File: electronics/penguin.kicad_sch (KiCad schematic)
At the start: 137 parts, among them IC1 HY2120-AB, J1 USB_C_CONN, J10 MTR_HEADER_2, J2 CAM_HEADER, J3 BATT_BALANCE_HEADER, J4 TOF_HEADER, J6 IR_HEADER_1, J7 IR_HEADER_2, J8 BATT_CONN, J9 MTR_HEADER_1, Q1 AO3400A, Q2 SI2393DS, Q3 2N7002, Q4 FS8205A, SW1 SW_Boot, SW2 SW_Reset, U1 ESP32-S3-WROOM-1U-N8R8, U2 LP5907MFX-2.8, U3 LP5907MFX-1.2, U4 DRV8833PW, U5 MCP23017_ML, U6 TPS5405DR, U7 AMS1117-3.3, U8 DMP4065S-7

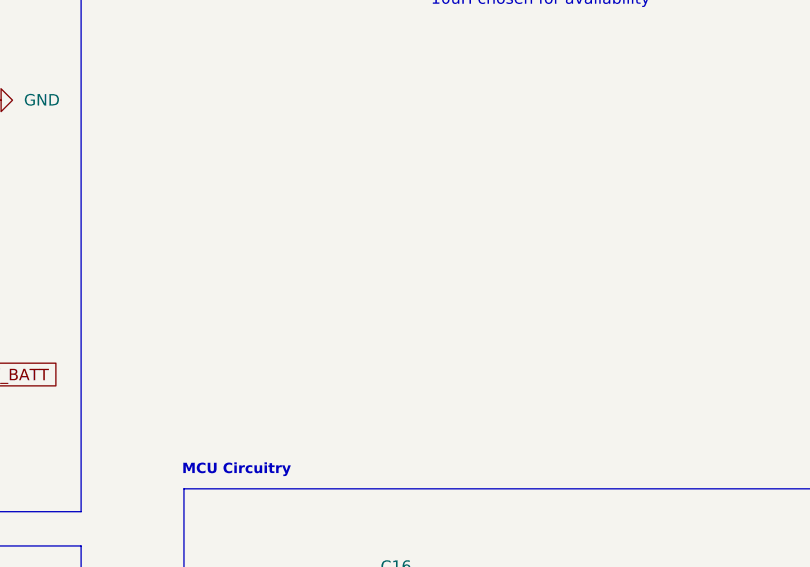
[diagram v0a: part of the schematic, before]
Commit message: finalize board outline
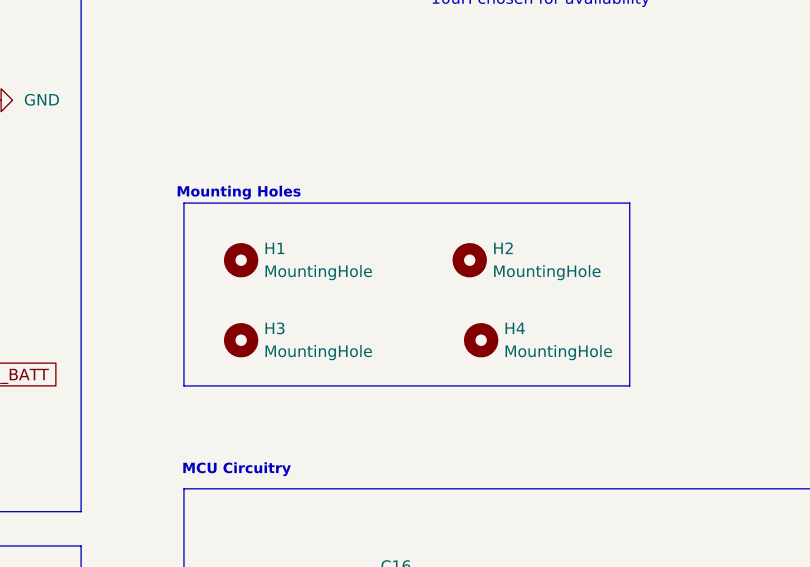
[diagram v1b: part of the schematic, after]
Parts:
- added H1, H2, H3, H4: MountingHole, MountingHole:MountingHole_2.2mm_M2, symbol Mechanical:MountingHole
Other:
- note added: "Mounting Holes"
- company: MREN 178 Course Project Extension -> Jeevan Sanchez
- title: P.A.N. Controller -> Penguin Controller

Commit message: silkscreen
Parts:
- C26: footprint Capacitor_SMD:C_0603_1608Metric -> Capacitor_SMD:C_0805_2012Metric; JLCPCB C14663 -> C49678
- C40: footprint EEH_ZK1V101XP:CAP_EEHZK1V101XP -> EEE_FK1V101P:CAP_EEEFK1V101P
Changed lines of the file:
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@@
 			)
 		)
-		(property "Footprint" "Capacitor_SMD:C_0603_1608Metric"
+		(property "Footprint" "Capacitor_SMD:C_0805_2012Metric"
 			(at 125.4252 86.36 0)
 			(effects
@@
 			)
 		)
-		(property "JLCPCB" "C14663"
+		(property "JLCPCB" "C49678"
 			(at 124.46 82.55 0)
 			(effects
@@
 			)
 		)
-		(property "Footprint" "EEH_ZK1V101XP:CAP_EEHZK1V101XP"
+		(property "Footprint" "EEE_FK1V101P:CAP_EEEFK1V101P"
 			(at 517.8552 69.85 0)
 			(effects

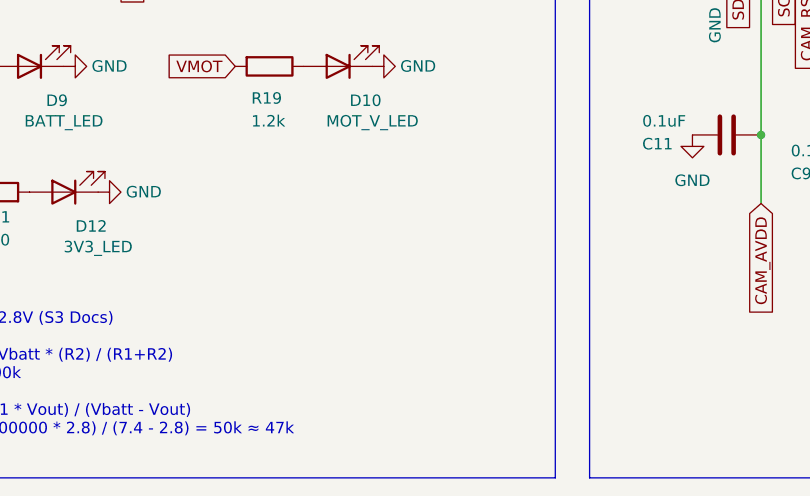
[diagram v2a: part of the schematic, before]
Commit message: finsih front silkscreen
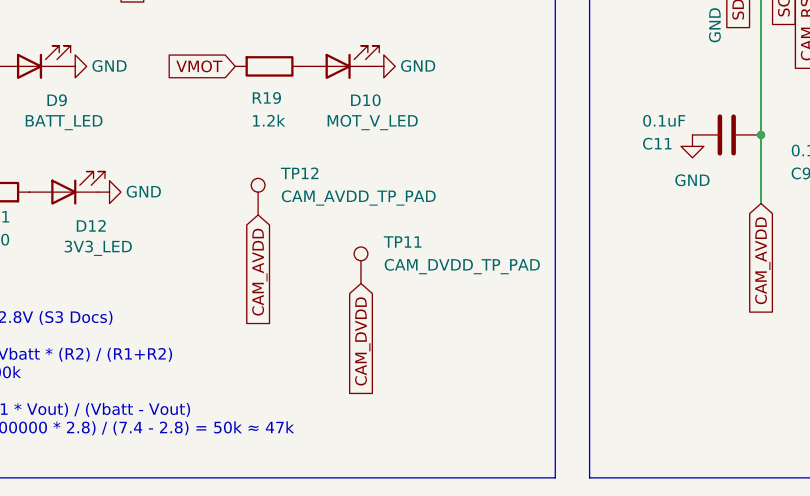
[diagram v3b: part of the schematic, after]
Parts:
- added TP11: CAM_DVDD_TP_PAD, TestPoint:TestPoint_Pad_1.0x1.0mm, symbol Connector:TestPoint
- added TP12: CAM_AVDD_TP_PAD, TestPoint:TestPoint_Pad_1.0x1.0mm, symbol Connector:TestPoint
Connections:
- net CAM_AVDD: now also TP12.1
- net CAM_DVDD: now also TP11.1

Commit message: add IMU and redo BMS pours
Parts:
- removed C47: 0.1uF, Capacitor_SMD:C_0603_1608Metric, symbol Device:C
- removed J6: IR_HEADER_1, MOLEX_NANO_4:CONN_SD-105313-100_04_MOL, symbol Connector_Generic:Conn_01x04
- removed J7: IR_HEADER_2, MOLEX_NANO_4:CONN_SD-105313-100_04_MOL, symbol Connector_Generic:Conn_01x04
- removed R30, R31: 200, Resistor_SMD:R_0603_1608Metric, symbol Device:R
- removed R32, R33: 10k, Resistor_SMD:R_0603_1608Metric, symbol Device:R
- added C13: 10uF, Capacitor_SMD:C_0805_2012Metric, symbol Device:C
- added J5, J6: I2C_JUMPER, Connector_PinHeader_1.27mm:PinHeader_1x04_P1.27mm_Vertical, symbol Connector:Conn_01x04_Pin
- added NT1: GND, NetTie:NetTie-2_SMD_Pad0.5mm, symbol Device:NetTie_2
- added U9: LSM6DSL, Package_LGA:LGA-14_3x2.5mm_P0.5mm_LayoutBorder3x4y, symbol Sensor_Motion:LSM6DSL
- C46: LCSC C14663 -> (none)
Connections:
- net IR_DATA_2 is gone; now on net CAM_VSYNC: U1.6 (IO6)
- net +3V3: now also C46.2, C13.1, J5.1 (Pin_1), J6.1 (Pin_1), U9.12 (CS), U9.5 (VDDIO), U9.8 (VDD); no longer C46.1
- net BATT_N: now also NT1.2; no longer C44.1, C45.1, IC1.6 (VSS), J3.1 (Pin_1)
- net BUZZ_EN: now also U5.21 (GPA4); no longer U5.17 (GPA0)
- net CAM_HREF: now also U1.7 (IO7); no longer U5.25 (GPB0)
- net CAM_PWDN_EN: now also U5.23 (GPA6); no longer U5.24 (GPA7)
- net CAM_RST: now also U5.24 (GPA7); no longer U5.26 (GPB1)
- net CAM_STATUS: now also U5.19 (GPA2); no longer U5.21 (GPA4)
- net CAM_VSYNC: no longer U5.23 (GPA6)
- net DBG_LED: now also R10.1, U5.17 (GPA0); no longer R9.1, U5.18 (GPA1)
- net GND: now also C46.1, C13.2, J5.2 (Pin_2), J6.2 (Pin_2), U9.1 (SDO/SA0), U9.2 (SDX), U9.3 (SCX), U9.6 (GND), U9.7 (GND); no longer C46.2
- net SCL: now also J5.4 (Pin_4), J6.4 (Pin_4), U9.13 (SCL)
- net SDA: now also J5.3 (Pin_3), J6.3 (Pin_3), U9.14 (SDA)
- net WIFI_LED: now also R9.1, U5.18 (GPA1); no longer R10.1, U5.19 (GPA2)
- net CAM_EN renamed CAM_PEN
- net IR_DATA_1 renamed IMU_INT
- net IMU_INT: now also U9.4 (INT1)
- new net VSS_SENSE: C44.1, C45.1, IC1.6 (VSS), J3.1 (Pin_1), NT1.1
- no-connect marks 15 -> 17
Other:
- note added: "IMU Interface"
- note removed: "TCRT5000 IR Sensors Interface"
- note removed: "The IR sensor is divided in two distinct sections The IR LED (Emitter) and the Phototransistor (Detector - The IR LED connections mirrors a regular LED circuit - The phototransistor circuit grounds the emitter to define a logic LOW. - When no IR light is reflected, the signal is pulled high - When IR light is reflected the PHT closes, shorting the signal LOW. - This transition is a definitive sig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"
